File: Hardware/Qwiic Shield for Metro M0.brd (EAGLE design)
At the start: 53.3 x 59.7 mm, 22 parts, among them Q1 BSS138, Q2 BSS138, U1 ARDUINO UNO

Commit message: Updated board/schematic
Changes are mostly to make the shield compatible with 3.3V logic
microcontrollers. This means there's no need for the level shifting
between the shield and the MCU. Also, the power lines are all connected
to the 3.3V pin instead of 5V.
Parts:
- removed Q1, Q2: BSS138, SparkFun-DiscreteSemi:SOT23-3
- removed R2, R3, R4, R5: 4.7K, SparkFun-Resistors:0603-RES
- removed U$1: SPARKX-LOGO3, SparkX:SPARKX-SMALL
- removed U$2: SPARKX-LOGO5, SparkX:SPARKX-LARGE
- moved LOGO1 42.0 mm to (5.08, 5.08)
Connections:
- removed net HV_SCL: J4.1, Q2.3, R5.2, U1.A5
- removed net HV_SDA: J4.2, Q1.3, R4.2, U1.A4
- net 3.3V: no longer Q1.1, Q2.1, R2.1, R3.1
- net 5V: no longer R4.1, R5.1
- net SCL: now also J4.1, U1.A5; no longer Q2.2, R2.2
- net SDA: now also J4.2, U1.A4; no longer Q1.2, R3.2
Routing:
- net 5V: track 129.8 -> 5.08 mm, vias 16 -> 0
- net 3.3V: track 79.8 -> 173.7 mm, vias 0 -> 16
- net HV_SCL: track 53.4 -> 0.00 mm, vias 1 -> 0
- net SDA: track 50.0 -> 99.0 mm
- net SCL: track 45.2 -> 93.7 mm, vias 5 -> 4
- net HV_SDA: track 47.6 -> 0.00 mm
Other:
- board text added: "3.3V"
- board text added: "M0.11"
- board text added: "Qwiic Shield for Metro M0"
- board text added: "RST"
- board text removed: "Qwiic Shield"
- board text removed: "RES"
- board text removed: "X11"

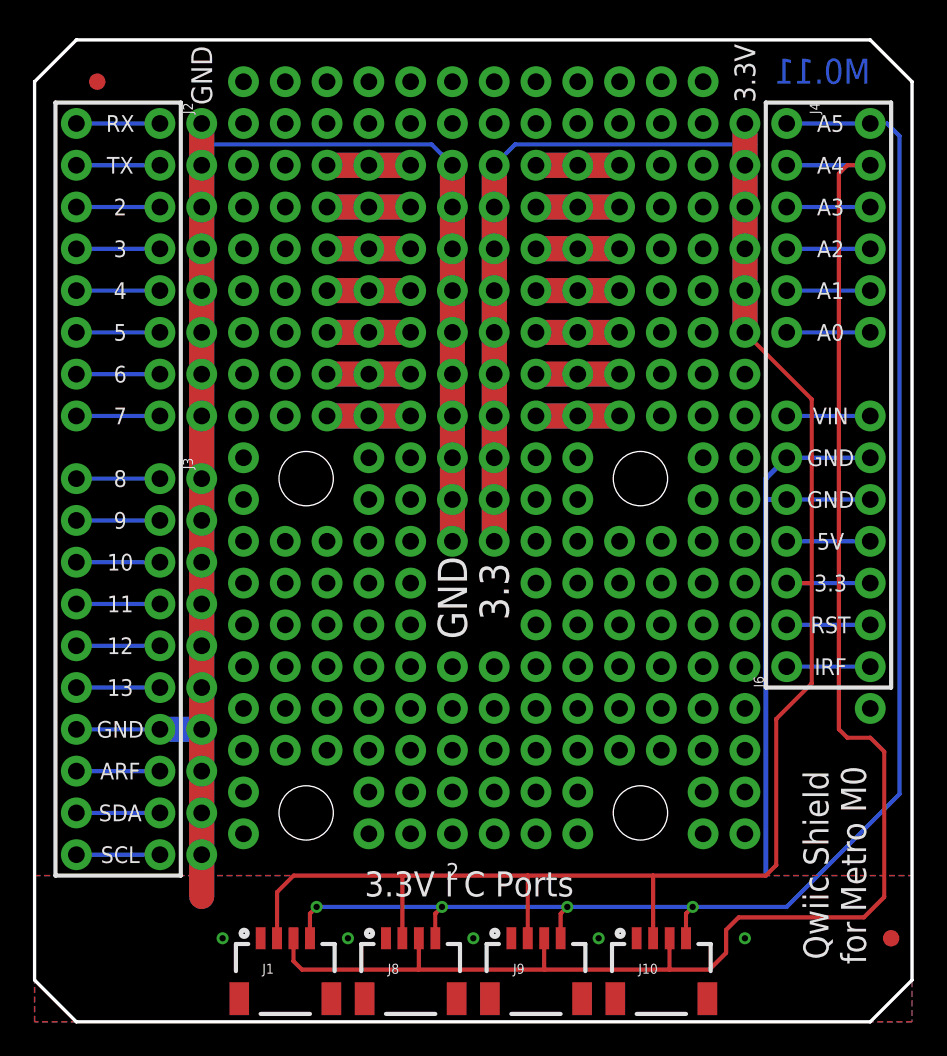
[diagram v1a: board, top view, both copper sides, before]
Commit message: Re-routed board to use SCL/SDA instead of A4/A5
The Metro Express M0 cannot use A4/A5 as SCL/SDA, so the previous
version of the shield was completely incompatible with the board.
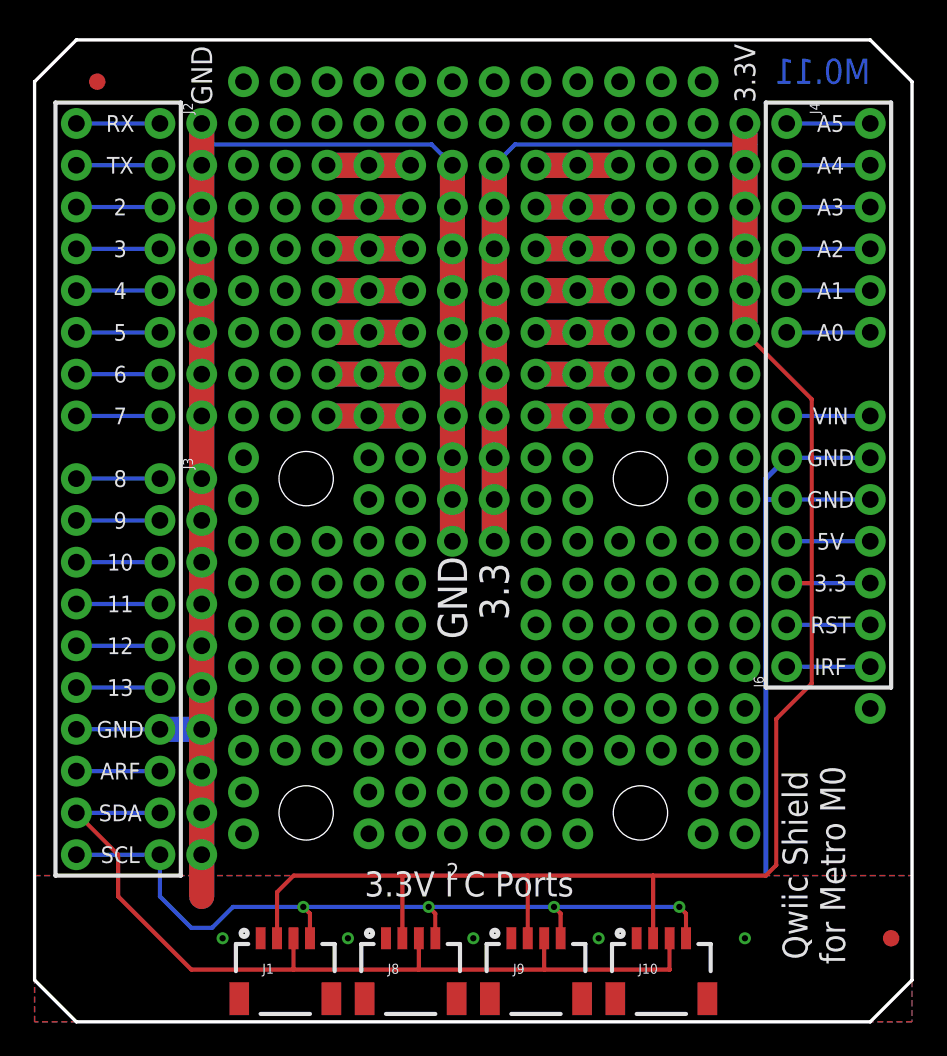
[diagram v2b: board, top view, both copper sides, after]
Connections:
- removed net SCL1: J3.10, U1.SCL
- removed net SDA1: J3.9, U1.SDA
- new net A4: J4.2, U1.A4
- new net A5: J4.1, U1.A5
- net SCL: now also J3.10, U1.SCL; no longer J4.1, U1.A5
- net SDA: now also J3.9, U1.SDA; no longer J4.2, U1.A4
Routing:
- net SCL: track 93.7 -> 48.8 mm
- net SDA: track 99.0 -> 54.2 mm
- net SDA1: track 5.08 -> 0.00 mm
- net SCL1: track 5.08 -> 0.00 mm
- net A5: track 0.00 -> 5.08 mm
- net A4: track 0.00 -> 5.08 mm
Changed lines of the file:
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@@
 <setting verticaltext="up"/>
 </settings>
-<grid distance="0.05" unitdist="inch" unit="inch" style="lines" multiple="1" display="yes" altdistance="0.005" altunitdist="inch" altunit="inch"/>
+<grid distance="0.05" unitdist="inch" unit="mm" style="lines" multiple="1" display="yes" altdistance="5" altunitdist="mil" altunit="mil"/>
 <layers>
 <layer number="1" name="Top" color="4" fill="1" visible="yes" active="yes"/>
@@
 <layer number="49" name="Reference" color="7" fill="1" visible="no" active="yes"/>
 <layer number="50" name="dxf" color="7" fill="1" visible="no" active="yes"/>
-<layer number="51" name="tDocu" color="6" fill="1" visible="yes" active="yes"/>
-<layer number="52" name="bDocu" color="7" fill="1" visible="yes" active="yes"/>
+<layer number="51" name="tDocu" color="6" fill="1" visible="no" active="yes"/>
+<layer number="52" name="bDocu" color="7" fill="1" visible="no" active="yes"/>
 <layer number="53" name="tGND_GNDA" color="7" fill="9" visible="no" active="no"/>
 <layer number="54" name="bGND_GNDA" color="1" fill="9" visible="no" active="no"/>
@@
 <wire x1="53.34" y1="2.54" x2="53.34" y2="57.15" width="0.2032" layer="20"/>
 <wire x1="0" y1="57.15" x2="0" y2="2.54" width="0.2032" layer="20"/>
-<text x="48.641" y="9.525" size="1.524" layer="21" font="vector" ratio="15" rot="R90" align="center">Qwiic Shield
+<text x="47.371" y="9.525" size="1.524" layer="21" font="vector" ratio="15" rot="R90" align="center">Qwiic Shield
 for Metro M0</text>
 <text x="22.86" y="-24.13" size="1.778" layer="51" font="vector" ratio="15">N. Seidle</text>
@@
 <dimension x1="0" y1="59.69" x2="53.34" y2="59.69" x3="26.67" y3="63.5" textsize="1.778" layer="20"/>
 <dimension x1="0" y1="59.69" x2="0" y2="0" x3="-3.81" y3="29.845" textsize="1.778" layer="20"/>
-<text x="48.641" y="9.525" size="1.524" layer="22" font="vector" ratio="15" rot="MR90" align="center">Qwiic Shield
+<text x="47.371" y="9.525" size="1.524" layer="22" font="vector" ratio="15" rot="MR270" align="center">Qwiic Shield
 for Metro M0</text>
 </plain>
@@
 <contactref element="J10" pad="4"/>
 <wire x1="39.6" y1="5.08" x2="39.6" y2="6.58" width="0.254" layer="1"/>
-<wire x1="39.6" y1="6.58" x2="40.005" y2="6.985" width="0.254" layer="1"/>
-<via x="40.005" y="6.985" extent="1-16" drill="0.381"/>
-<wire x1="45.72" y1="6.985" x2="40.005" y2="6.985" width="0.254" layer="16"/>
+<wire x1="39.6" y1="6.58" x2="39.195" y2="6.985" width="0.254" layer="1"/>
+<via x="39.195" y="6.985" extent="1-16" drill="0.381"/>
 <wire x1="31.98" y1="5.08" x2="31.98" y2="6.58" width="0.254" layer="1"/>
-<wire x1="31.98" y1="6.58" x2="32.385" y2="6.985" width="0.254" layer="1"/>
-<via x="32.385" y="6.985" extent="1-16" drill="0.381"/>
-<wire x1="32.385" y1="6.985" x2="40.005" y2="6.985" width="0.254" layer="16"/>
+<wire x1="31.98" y1="6.58" x2="31.575" y2="6.985" width="0.254" layer="1"/>
+<via x="31.575" y="6.985" extent="1-16" drill="0.381"/>
+<wire x1="31.575" y1="6.985" x2="39.195" y2="6.985" width="0.254" layer="16"/>
 <wire x1="24.36" y1="5.08" x2="24.36" y2="6.58" width="0.254" layer="1"/>
-<wire x1="24.36" y1="6.58" x2="24.765" y2="6.985" width="0.254" layer="1"/>
-<via x="24.765" y="6.985" extent="1-16" drill="0.381"/>
-<wire x1="24.765" y1="6.985" x2="32.385" y2="6.985" width="0.254" layer="16"/>
+<wire x1="24.36" y1="6.58" x2="23.955" y2="6.985" width="0.254" layer="1"/>
+<via x="23.955" y="6.985" extent="1-16" drill="0.381"/>
+<wire x1="23.955" y1="6.985" x2="31.575" y2="6.985" width="0.254" layer="16"/>
 <wire x1="16.74" y1="5.08" x2="16.74" y2="6.58" width="0.254" layer="1"/>
-<wire x1="16.74" y1="6.58" x2="17.145" y2="6.985" width="0.254" layer="1"/>
-<via x="17.145" y="6.985" extent="1-16" drill="0.381"/>
-<wire x1="17.145" y1="6.985" x2="24.765" y2="6.985" width="0.254" layer="16"/>
-<contactref element="U1" pad="A5"/>
-<contactref element="J4" pad="1"/>
-<wire x1="50.8" y1="54.61" x2="45.72" y2="54.61" width="0.254" layer="16"/>
-<wire x1="51.816" y1="54.61" x2="52.578" y2="53.848" width="0.254" layer="16"/>
-<wire x1="51.816" y1="54.61" x2="50.8" y2="54.61" width="0.254" layer="16"/>
-<wire x1="52.578" y1="13.843" x2="45.72" y2="6.985" width="0.254" layer="16"/>
-<wire x1="52.578" y1="53.848" x2="52.578" y2="13.843" width="0.254" layer="16"/>
+<wire x1="16.74" y1="6.58" x2="16.335" y2="6.985" width="0.254" layer="1"/>
+<via x="16.335" y="6.985" extent="1-16" drill="0.381"/>
+<wire x1="23.955" y1="6.985" x2="16.335" y2="6.985" width="0.254" layer="16"/>
+<wire x1="16.335" y1="6.985" x2="12.065" y2="6.985" width="0.254" layer="16"/>
+<wire x1="12.065" y1="6.985" x2="10.795" y2="5.715" width="0.254" layer="16"/>
+<wire x1="10.795" y1="5.715" x2="9.525" y2="5.715" width="0.254" layer="16"/>
+<wire x1="9.525" y1="5.715" x2="7.62" y2="7.62" width="0.254" layer="16"/>
+<contactref element="J3" pad="10"/>
+<contactref element="U1" pad="SCL"/>
+<wire x1="7.62" y1="10.16" x2="2.54" y2="10.16" width="0.254" layer="16"/>
+<wire x1="7.62" y1="7.62" x2="7.62" y2="10.16" width="0.254" layer="16"/>
 </signal>
 <signal name="SDA">
@@
 <contactref element="J9" pad="3"/>
 <contactref element="J10" pad="3"/>
-<wire x1="15.74" y1="5.08" x2="15.74" y2="3.691" width="0.254" layer="1"/>
-<wire x1="15.74" y1="3.691" x2="16.256" y2="3.175" width="0.254" layer="1"/>
-<wire x1="16.256" y1="3.175" x2="23.368" y2="3.175" width="0.254" layer="1"/>
-<wire x1="23.368" y1="3.175" x2="30.988" y2="3.175" width="0.254" layer="1"/>
+<wire x1="15.74" y1="5.08" x2="15.74" y2="3.175" width="0.254" layer="1"/>
+<wire x1="30.988" y1="3.175" x2="23.368" y2="3.175" width="0.254" layer="1"/>
 <wire x1="30.988" y1="3.175" x2="38.608" y2="3.175" width="0.254" layer="1"/>
-<wire x1="38.608" y1="3.175" x2="41.021" y2="3.175" width="0.254" layer="1"/>
-<wire x1="41.021" y1="3.175" x2="42.037" y2="4.191" width="0.254" layer="1"/>
-<wire x1="42.037" y1="4.191" x2="42.037" y2="5.588" width="0.254" layer="1"/>
-<wire x1="42.037" y1="5.588" x2="42.799" y2="6.35" width="0.254" layer="1"/>
-<wire x1="42.799" y1="6.35" x2="50.419" y2="6.35" width="0.254" layer="1"/>
-<wire x1="50.419" y1="6.35" x2="51.65" y2="7.581" width="0.254" layer="1"/>
 <wire x1="38.6" y1="5.08" x2="38.6" y2="3.183" width="0.254" layer="1"/>
 <wire x1="38.6" y1="3.183" x2="38.608" y2="3.175" width="0.254" layer="1"/>
@@
 <wire x1="23.36" y1="5.08" x2="23.36" y2="3.183" width="0.254" layer="1"/>
 <wire x1="23.36" y1="3.183" x2="23.368" y2="3.175" width="0.254" layer="1"/>
-<contactref element="U1" pad="A4"/>
-<contactref element="J4" pad="2"/>
-<wire x1="45.72" y1="52.07" x2="50.8" y2="52.07" width="0.254" layer="16"/>
-<wire x1="51.65" y1="16.422" x2="50.8" y2="17.272" width="0.254" layer="1"/>
-<wire x1="50.8" y1="17.272" x2="49.403" y2="17.272" width="0.254" layer="1"/>
-<wire x1="49.403" y1="17.272" x2="48.895" y2="17.78" width="0.254" layer="1"/>
-<wire x1="48.895" y1="17.78" x2="48.895" y2="51.562" width="0.254" layer="1"/>
-<wire x1="48.895" y1="51.562" x2="49.403" y2="52.07" width="0.254" layer="1"/>
-<wire x1="49.403" y1="52.07" x2="50.8" y2="52.07" width="0.254" layer="1"/>
-<wire x1="51.65" y1="7.581" x2="51.65" y2="16.422" width="0.254" layer="1"/>
+<wire x1="23.368" y1="3.175" x2="15.74" y2="3.175" width="0.254" layer="1"/>
+<wire x1="15.74" y1="3.175" x2="9.525" y2="3.175" width="0.254" layer="1"/>
+<wire x1="9.525" y1="3.175" x2="5.08" y2="7.62" width="0.254" layer="1"/>
+<wire x1="5.08" y1="7.62" x2="5.08" y2="10.16" width="0.254" layer="1"/>
+<contactref element="U1" pad="SDA"/>
+<contactref element="J3" pad="9"/>
+<wire x1="2.54" y1="12.7" x2="7.62" y2="12.7" width="0.254" layer="16"/>
+<wire x1="5.08" y1="10.16" x2="2.54" y2="12.7" width="0.254" layer="1"/>
 </signal>
 <signal name="5V">
@@
 <contactref element="J6" pad="7"/>
 <wire x1="45.72" y1="36.83" x2="50.8" y2="36.83" width="0.254" layer="16"/>
-</signal>
-<signal name="SCL1">
-<contactref element="J3" pad="10"/>
-<contactref element="U1" pad="SCL"/>
-<wire x1="7.62" y1="10.16" x2="2.54" y2="10.16" width="0.254" layer="16"/>
-</signal>
-<signal name="SDA1">
-<contactref element="U1" pad="SDA"/>
-<contactref element="J3" pad="9"/>
-<wire x1="2.54" y1="12.7" x2="7.62" y2="12.7" width="0.254" layer="16"/>
 </signal>
 <signal name="CH1">
@@
 <via x="27.94" y="54.61" extent="1-16" drill="1.016" diameter="1.8796"/>
 </signal>
+<signal name="A5">
+<contactref element="U1" pad="A5"/>
+<contactref element="J4" pad="1"/>
+<wire x1="50.8" y1="54.61" x2="45.72" y2="54.61" width="0.254" layer="16"/>
+</signal>
+<signal name="A4">
+<contactref element="U1" pad="A4"/>
+<contactref element="J4" pad="2"/>
+<wire x1="45.72" y1="52.07" x2="50.8" y2="52.07" width="0.254" layer="16"/>
+</signal>
 </signals>
